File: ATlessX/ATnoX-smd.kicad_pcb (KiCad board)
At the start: 4 copper layers, 80 x 47 mm, 41 parts, among them J1 EXT_PWR_SW, J2 ATX, J3 AT, J4 PWR_LED, SW1 Power, U1 74LS74, U2 74LS14, U3 L7905, U4 74HCT4060, U5 74HC73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

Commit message: Add thermal relief pads
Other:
- board text added: "Power Adapter Cable"
- board text removed: "AT Power Connector"
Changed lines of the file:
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@@
   (page A4)
   (layers
-    (0 F.Cu signal)
-    (1 In1.Cu power)
-    (2 In2.Cu power)
-    (31 B.Cu signal)
-    (32 B.Adhes user)
-    (33 F.Adhes user)
+    (0 F.Cu signal hide)
+    (1 In1.Cu power hide)
+    (2 In2.Cu power hide)
+    (31 B.Cu signal hide)
+    (32 B.Adhes user hide)
+    (33 F.Adhes user hide)
     (34 B.Paste user)
     (35 F.Paste user hide)
@@
     (effects (font (size 1 1) (thickness 0.15)) (justify mirror))
   )
-  (gr_text "AT  Power Connector" (at 146.05 113.03) (layer B.SilkS)
+  (gr_text "Power Adapter Cable" (at 146.05 113.03) (layer B.SilkS)
     (effects (font (size 1 1) (thickness 0.15)) (justify mirror))
   )
@@
   )
   (zone (net 1) (net_name GND) (layer B.Cu) (hatch edge 0.508)
-    (connect_pads yes (clearance 0.508))
+    (connect_pads (clearance 0.508))
     (min_thickness 0.254)
     (fill yes (arc_segments 32) (thermal_gap 0.508) (thermal_bridge_width 0.508))
@@
   )
   (zone (net 1) (net_name GND) (layer F.Cu) (hatch edge 0.508)
-    (connect_pads yes (clearance 0.508))
+    (connect_pads (clearance 0.508))
     (min_thickness 0.254)
     (fill yes (arc_segments 32) (thermal_gap 0.508) (thermal_bridge_width 0.508))

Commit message: Add silkscreen text
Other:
- board text added: "74HCT4060"
- board text added: "74HCT73"

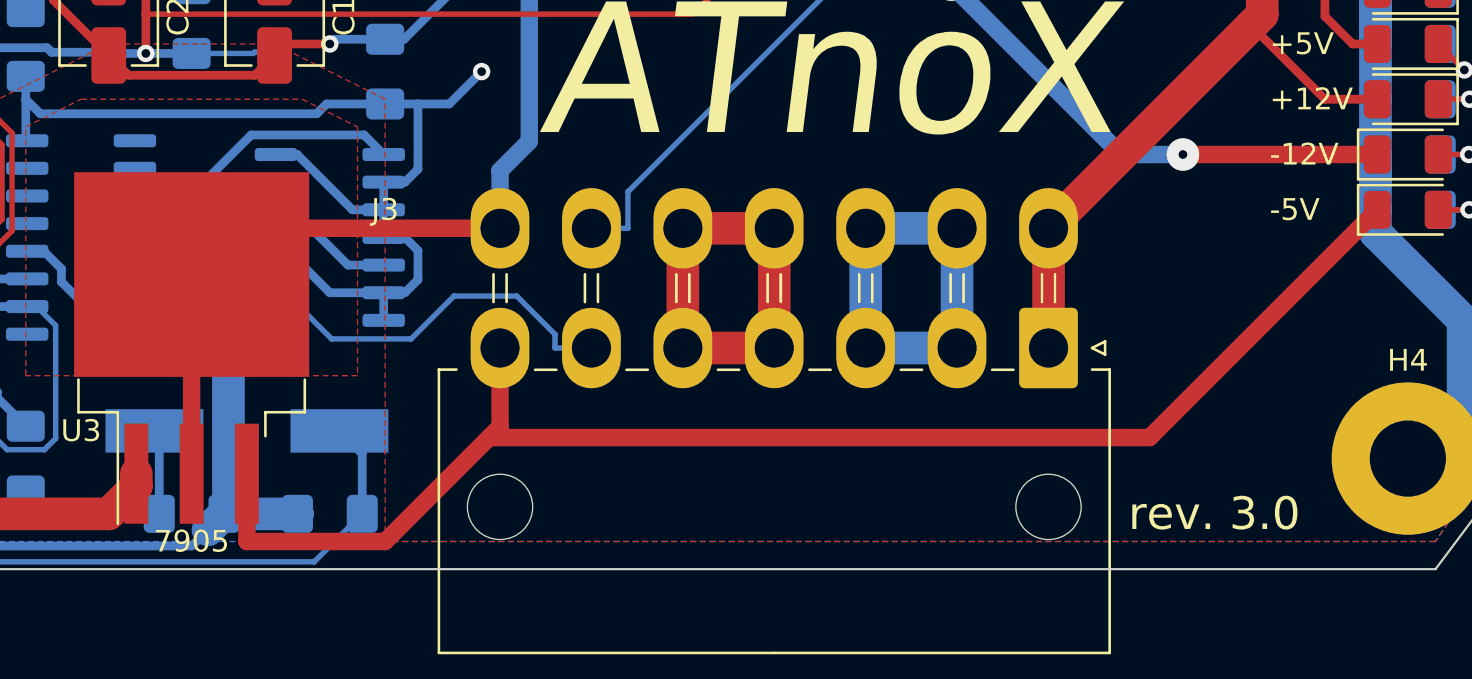
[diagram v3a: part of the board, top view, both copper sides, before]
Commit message: Removed old versions, fix wrong pin connected to 4, rev 3.1
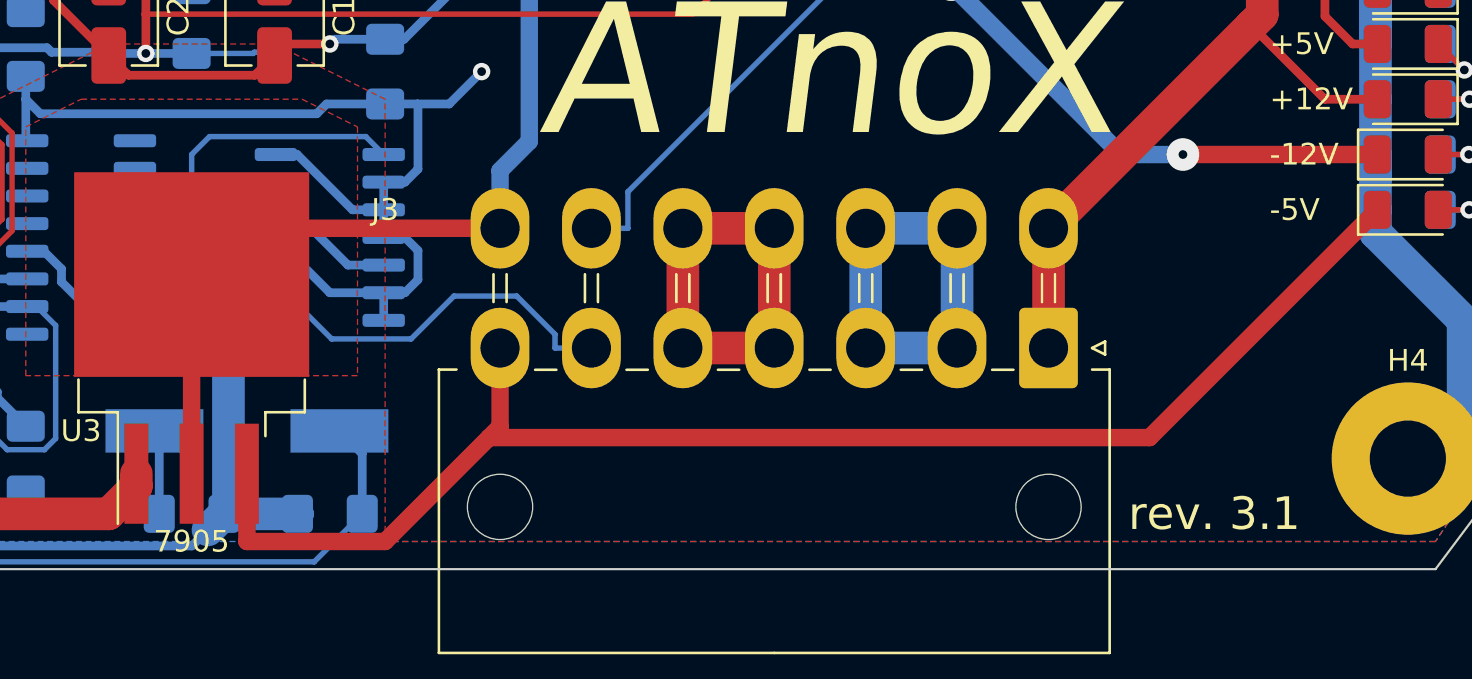
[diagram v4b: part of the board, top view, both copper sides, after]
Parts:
- U5: value 74HC73 -> 74HCT73
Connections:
- U4 pad 3: (no net) -> Net-(U4-Pad3)
- U4 pad 7: Net-(U4-Pad7) -> (no net)
- U5 pad 1: Net-(U4-Pad7) -> Net-(U4-Pad3)
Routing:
- net Net-(U4-Pad7): track 18.2 -> 0.00 mm
- net Net-(U4-Pad3): track 0.00 -> 14.4 mm
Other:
- board text added: "74HC4060"
- board text added: "74HC73"
- board text added: "rev. 3.1"
- board text removed: "74HCT4060"
- board text removed: "74HCT73"
- board text removed: "rev. 3.0"

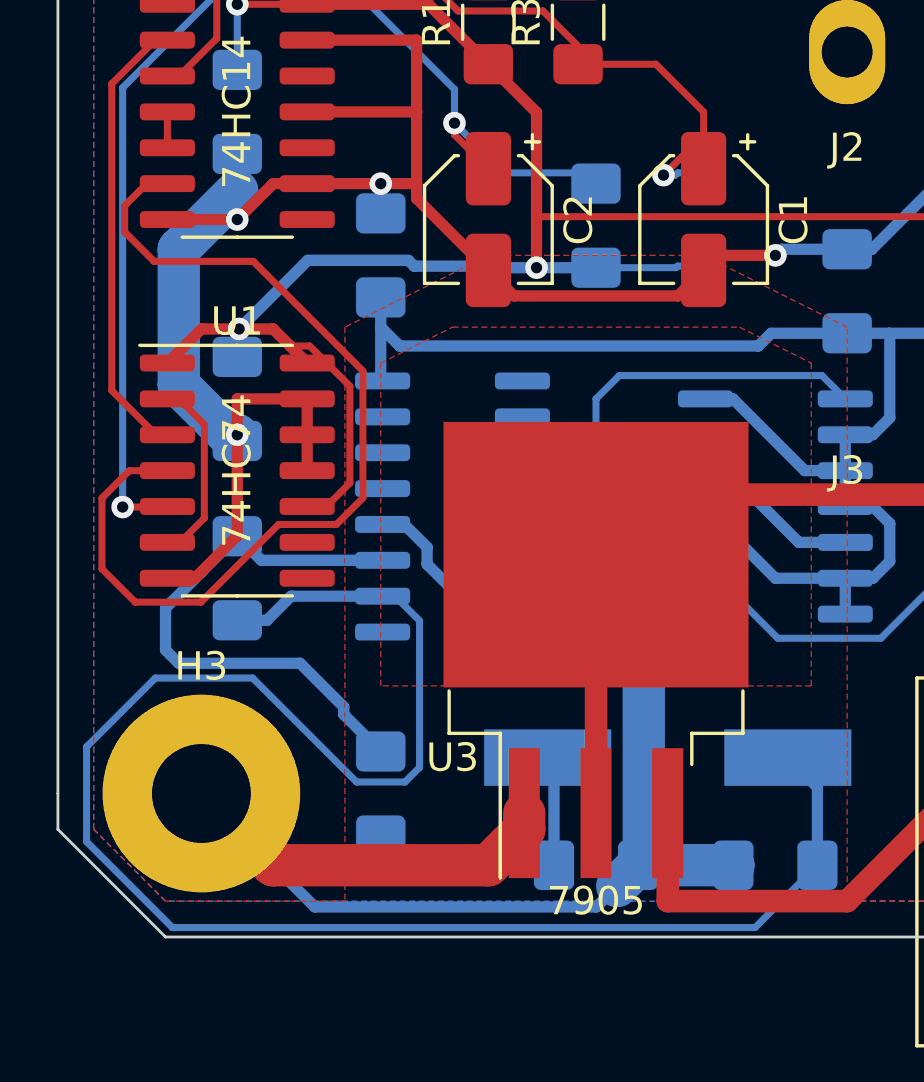
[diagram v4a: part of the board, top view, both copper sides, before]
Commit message: Fix paths and update gerbers
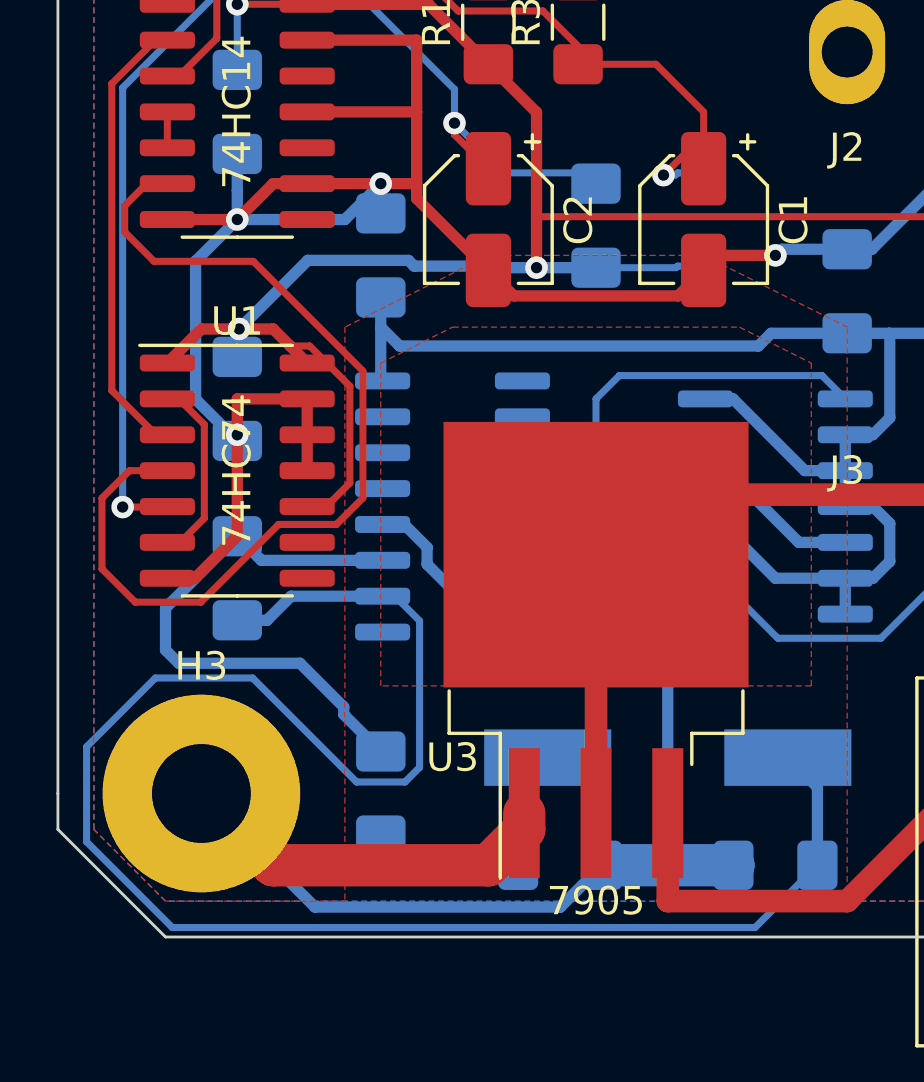
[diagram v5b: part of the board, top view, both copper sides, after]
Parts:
- moved C7 1.27 mm to (118.1, 111.8)
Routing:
- net GND: track 415.2 -> 418.7 mm
- net Net-(C7-Pad1): track 10.5 -> 9.86 mm
